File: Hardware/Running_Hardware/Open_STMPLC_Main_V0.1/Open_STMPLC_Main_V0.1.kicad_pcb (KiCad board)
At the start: 4 copper layers, 168.8 x 90 mm, 184 parts, among them J1 Conn_02x08_Odd_Even, J10 10144518-041802LF, J12 USB C, J13 RJ45_Hanrun_HR911105A_Horizon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, J2 USB C, J3 Conn_01x04, J4 TF-01A, J5 Conn_Coaxial, J6 Conn_Coaxial, J7 Simcard_Nano, J8 10144518-041802LF, J9 10144518-041802LF, Q1 DTC143Z, Q2 DTC143Z, Q3 DTC143Z, Q4 DTC143Z, Q5 DTC143Z, Q6 DTC143Z, Q7 DTC143Z, Q8 DTC143Z, SW1 Switch_6x6, SW2 SW_DIP_x01, SW3 Switch_6x6, U1 STM32F407IGTx, U10 AP63205WU, U2 ADM2587E, U3 TPS3430WDRC, U4 CH340C, U5 AMS1117-3.3, U6 W25Q64JVSSIQ, U7 LAN8720A, U8 EC200U, U9 AP63200WU, Y1 48MHz, Y2 32.768kHz, Y3 25MHz

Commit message: PCB routing completion v0.1 Main
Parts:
- added C73: 1nF/2kV, Capacitor_SMD:C_1206_3216Metric_Pad1.33x1.80mm_HandSolder, F.Cu at (209.0, 74.5)
- added D10: UAD8C05L01, Diode_SMD:D_SOD-882, F.Cu at (128.5, 72.0)
- added D11: UAD8C05L01, Diode_SMD:D_SOD-882, F.Cu at (136.5, 72.0)
- added D12: UAD8C05L01, Diode_SMD:D_SOD-882, F.Cu at (134.5, 72.0)
- added D13: UAD8C05L01, Diode_SMD:D_SOD-882, F.Cu at (144.5, 72.0)
- added D14: UAD8C05L01, Diode_SMD:D_SOD-882, F.Cu at (188.0, 66.0)
- added D15: UAD8C05L01, Diode_SMD:D_SOD-882, F.Cu at (185.5, 66.0)
- added D16: UAD8C05L01, Diode_SMD:D_SOD-882, F.Cu at (183.0, 66.0)
- added D17: UAD8C05L01, Diode_SMD:D_SOD-882, F.Cu at (180.5, 66.0)
- added D18: UAD8C05L01, Diode_SMD:D_SOD-882, F.Cu at (178.0, 66.0)
- added D19: UAD8C05L01, Diode_SMD:D_SOD-882, F.Cu at (142.5, 72.0)
- added D20: UAD8C05L01, Diode_SMD:D_SOD-882, F.Cu at (175.5, 66.0)
- added D21: UAD8C05L01, Diode_SMD:D_SOD-882, F.Cu at (173.0, 66.0)
- added D22: UAD8C05L01, Diode_SMD:D_SOD-882, F.Cu at (173.0, 68.2)
- added D23: UAD8C05L01, Diode_SMD:D_SOD-882, F.Cu at (175.5, 68.0)
- added D24: UAD8C05L01, Diode_SMD:D_SOD-882, F.Cu at (178.0, 68.0)
- added D25: UAD8C05L01, Diode_SMD:D_SOD-882, F.Cu at (180.5, 68.0)
- added D26: UAD8C05L01, Diode_SMD:D_SOD-882, F.Cu at (183.0, 68.0)
- added D27: UAD8C05L01, Diode_SMD:D_SOD-882, F.Cu at (185.5, 68.0)
- added D28: UAD8C05L01, Diode_SMD:D_SOD-882, F.Cu at (188.0, 68.0)
- added D29: UAD8C05L01, Diode_SMD:D_SOD-882, F.Cu at (199.0, 63.5)
- added D30: UAD8C05L01, Diode_SMD:D_SOD-882, F.Cu at (192.5, 63.5)
- added D31: UAD8C05L01, Diode_SMD:D_SOD-882, F.Cu at (195.0, 63.5)
- added D5: UAD8C05L01, Diode_SMD:D_SOD-882, F.Cu at (140.5, 72.0)
- added D9: UAD8C05L01, Diode_SMD:D_SOD-882, F.Cu at (130.5, 72.0)
- added FID1: Fiducial, Fiducial:Fiducial_1mm_Mask3mm, F.Cu at (53.0, 58.0)
- added FID2: Fiducial, Fiducial:Fiducial_1mm_Mask3mm, F.Cu at (213.0, 58.0)
- added FID3: Fiducial, Fiducial:Fiducial_1mm_Mask3mm, F.Cu at (206.0, 137.0)
- added FID4: Fiducial, Fiducial:Fiducial_1mm_Mask3mm, F.Cu at (53.0, 133.0)
- added R48: 10K, Resistor_SMD:R_0603_1608Metric_Pad0.98x0.95mm_HandSolder, F.Cu at (181.0, 95.5)
- added R49: 10K, Resistor_SMD:R_0603_1608Metric_Pad0.98x0.95mm_HandSolder, F.Cu at (181.0, 93.5)
- added R50: 4.7K, Resistor_SMD:R_0603_1608Metric_Pad0.98x0.95mm_HandSolder, F.Cu at (192.5, 66.5)
- added R51: 4.7K, Resistor_SMD:R_0603_1608Metric_Pad0.98x0.95mm_HandSolder, F.Cu at (195.0, 66.5)
- added R52: 4.7K, Resistor_SMD:R_0603_1608Metric_Pad0.98x0.95mm_HandSolder, F.Cu at (184.5, 71.0)
- added R53: 4.7K, Resistor_SMD:R_0603_1608Metric_Pad0.98x0.95mm_HandSolder, F.Cu at (187.0, 71.0)
- added U11: SRV05-4, Package_TO_SOT_SMD:SOT-23-6, F.Cu at (152.0, 61.5)
- added U12: SRV05-4, Package_TO_SOT_SMD:SOT-23-6, F.Cu at (164.0, 61.5)
- D2, D3, D4, D7, D8: value SMF5V0A -> UAD8C05L01; footprint Diode_SMD:D_SMF -> Diode_SMD:D_SOD-882
- D6: value DT1240A-08LP3810 -> UAD8C05L01; footprint Package_DFN_QFN:UDFN-9_1.0x3.8mm_P0.5mm -> Diode_SMD:D_SOD-882
- R30: value 10K -> 1M; footprint Resistor_SMD:R_0603_1608Metric_Pad0.98x0.95mm_HandSolder -> Resistor_SMD:R_1206_3216Metric_Pad1.30x1.75mm_HandSolder
- U7: footprint Package_DFN_QFN:VQFN-24-1EP_4x4mm_P0.5mm_EP2.5x2.5mm_ThermalVias -> Package_DFN_QFN:VQFN-24-1EP_4x4mm_P0.5mm_EP2.5x2.5mm
- moved R17 35.6 mm to (209.5, 97.5), turned to 0 degrees
- moved R30 15.7 mm to (205.0, 74.5)
- moved R32 8.51 mm to (159.0, 61.5)
- moved R25 7.65 mm to (197.5, 82.5), turned to 90 degrees
- moved R40 6.73 mm to (173.0, 71.0)
- moved C41 5.52 mm to (195.5, 82.5), turned to -90 degrees
- moved R23 5.52 mm to (195.5, 88.5), turned to 90 degrees
- moved R34 5.40 mm to (112.2, 70.8)
- moved D6 5.39 mm to (132.5, 72.0), turned to 90 degrees
- moved R41 4.92 mm to (178.0, 71.0)
- moved R39 4.53 mm to (175.5, 71.0)
- moved C71 4.30 mm to (114.0, 98.5), turned to 0 degrees
- moved C49 3.95 mm to (115.8, 70.8)
- moved C50 3.95 mm to (121.8, 70.8)
- moved C52 3.95 mm to (117.8, 70.8)
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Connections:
- net Net-(J5-In) renamed /GSM_Module/ANT_GNSS
- net Net-(J6-In) renamed /GSM_Module/ANT_MAIN
- D2 pad 1: /GSM_Module/USIM_DATA -> GND
- D2 pad 2: GND -> /GSM_Module/USIM_DATA
- D3 pad 1: /GSM_Module/USIM_DET -> GND
- D3 pad 2: GND -> /GSM_Module/USIM_DET
- D4 pad 1: /GSM_Module/USIM_RST -> GND
- D4 pad 2: GND -> /GSM_Module/USIM_RST
- D6 pad 1: /SD_DAT1 -> GND
- D6 pad 2: /SD_DAT0 -> /SD_CMD
- D7 pad 1: /GSM_Module/USIM_VDD -> GND
- D7 pad 2: GND -> /GSM_Module/USIM_VDD
- D8 pad 1: /GSM_Module/USIM_CLK -> GND
- D8 pad 2: GND -> /GSM_Module/USIM_CLK
- J1 pad 11: /Microcontroller/EX_SPI_CLK -> /Microcontroller/EX_SPI_MISO
- J1 pad 12: /Microcontroller/EX_GPIO2 -> /Microcontroller/EX_SPI_CLK
- J1 pad 13: unconnected-(J1-Pin_13-Pad13) -> /Microcontroller/EX_UART_RX
- J1 pad 14: unconnected-(J1-Pin_14-Pad14) -> /Microcontroller/EX_UART_TX
- J1 pad 2: +3V3 -> +5V
- J1 pad 3: /Microcontroller/EX_I2C_SDA -> /Microcontroller/EX_I2C_SCL
- J1 pad 4: unconnected-(J1-Pin_4-Pad4) -> /Microcontroller/EX_I2C_SDA
- J1 pad 5: /Microcontroller/EX_I2C_SCL -> /Microcontroller/EX_GPIO4
- J1 pad 6: /Microcontroller/EX_UART_TX -> /Microcontroller/EX_GPIO5
- J1 pad 7: /Microcontroller/EX_SPI_MOSI -> /Microcontroller/EX_GPIO2
- J1 pad 8: /Microcontroller/EX_UART_RX -> /Microcontroller/EX_GPIO3
- J1 pad 9: /Microcontroller/EX_SPI_MISO -> /Microcontroller/EX_SPI_MOSI
- J12 pad A4: Net-(J12-VBUS-PadA4) -> VBUS
- J12 pad A9: Net-(J12-VBUS-PadA4) -> VBUS
- J12 pad B4: Net-(J12-VBUS-PadA4) -> VBUS
- J12 pad B9: Net-(J12-VBUS-PadA4) -> VBUS
- J13 pad 10: /Ethernet/LED2 -> GND
- J13 pad 11: /Ethernet/LED1 -> GND
- J13 pad 8: Earth -> Net-(C73-Pad1)
- J13 pad SH: GND -> Net-(C73-Pad1)
- J2 pad A4: Net-(J2-VBUS-PadA4) -> VBUS
- J2 pad A9: Net-(J2-VBUS-PadA4) -> VBUS
- J2 pad B4: Net-(J2-VBUS-PadA4) -> VBUS
- J2 pad B9: Net-(J2-VBUS-PadA4) -> VBUS
- R17 pad 1: /Microcontroller/DISP_SCL -> GND
- R17 pad 2: +3V3 -> /Ethernet/LED2
- R27 pad 2: +3V3 -> /Ethernet/LED1
- R28 pad 2: +3V3 -> /Ethernet/LED2
- R30 pad 1: /Microcontroller/DISP_SDA -> GND
- R30 pad 2: +3V3 -> Net-(C73-Pad1)
- R32 pad 1: Net-(J12-VBUS-PadA4) -> VBUS
- R9 pad 1: Net-(J2-VBUS-PadA4) -> VBUS
- U1 pad 100: unconnected-(U1-PD12-Pad100) -> /GSM_Module/RESET_IN
- U1 pad 101: unconnected-(U1-PD13-Pad101) -> /GSM_Module/PWRKEY_IN
- U1 pad 104: unconnected-(U1-PD14-Pad104) -> /SD_DET
- U1 pad 45: /B2B_Connector/DIG_OUT_5 -> /Microcontroller/EX_I2C_SCL
- U1 pad 46: /B2B_Connector/DIG_OUT_~{FAULT}_7 -> /Microcontroller/EX_I2C_SDA
- U1 pad 7: unconnected-(U1-PI8-Pad7) -> /Microcontroller/WDI
- U1 pad 77: unconnected-(U1-PE14-Pad77) -> /MODBUS/RS485_DE
- U1 pad 78: unconnected-(U1-PE15-Pad78) -> /MODBUS/RS485_~{RE}
- U1 pad 83: unconnected-(U1-PH6-Pad83) -> /B2B_Connector/DIG_OUT_~{FAULT}_7
- U1 pad 84: unconnected-(U1-PH7-Pad84) -> /Microcontroller/DISP_SCL
- U1 pad 85: unconnected-(U1-PH8-Pad85) -> /Microcontroller/DISP_SDA
- U1 pad 86: unconnected-(U1-PH9-Pad86) -> /B2B_Connector/DIG_OUT_5
- U1 pad 87: unconnected-(U1-PH10-Pad87) -> /Microcontroller/EX_GPIO5
- U1 pad 88: unconnected-(U1-PH11-Pad88) -> /Microcontroller/EX_GPIO4
- U1 pad 89: unconnected-(U1-PH12-Pad89) -> /Microcontroller/EX_GPIO3
- U1 pad 92: unconnected-(U1-PB12-Pad92) -> /Microcontroller/EX_GPIO2
- U1 pad 93: unconnected-(U1-PB13-Pad93) -> /Microcontroller/EX_GPIO1
- U1 pad 96: unconnected-(U1-PD8-Pad96) -> /Microcontroller/Flash_Hold
- U1 pad 97: unconnected-(U1-PD9-Pad97) -> /Microcontroller/Flash_CS
- U1 pad 98: unconnected-(U1-PD10-Pad98) -> /Microcontroller/Flash_WP
- U1 pad 99: unconnected-(U1-PD11-Pad99) -> /GSM_Module/GSM_BOOT
- U7 pad 10: /Ethernet/ETH_RXER -> /Ethernet/PHYAD0
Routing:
- net +3V3: track 22.9 -> 364.5 mm, vias 0 -> 20
- net +5V: track 18.1 -> 250.7 mm, vias 0 -> 3
- net /Microcontroller/3V3_MCU: track 89.2 -> 245.8 mm, vias 0 -> 4
- net /GSM_Module/GSM_DN: track 0.00 -> 117.3 mm, vias 0 -> 2
- net /GSM_Module/GSM_DP: track 0.00 -> 117.2 mm, vias 0 -> 2
- net /GSM_Module/SIM_TX: track 5.05 -> 94.3 mm, vias 1 -> 2
- net /GSM_Module/SIM_RX: track 4.40 -> 84.6 mm, vias 1 -> 2
- net GND: track 4.40 -> 79.4 mm, vias 0 -> 202
- net /Microcontroller/EX_I2C_SDA: track 0.00 -> 71.4 mm, vias 0 -> 2
- net /Microcontroller/EX_I2C_SCL: track 0.00 -> 69.1 mm, vias 0 -> 2
- net +24V: track 20.6 -> 88.0 mm, vias 1 -> 3
- net Net-(J13-RCT): track 0.00 -> 64.3 mm, vias 0 -> 5
- net /GSM_Module/PWRKEY_IN: track 0.00 -> 63.1 mm, vias 0 -> 2
- net /GSM_Module/RESET_IN: track 0.00 -> 60.6 mm, vias 0 -> 2
- net /GSM_Module/GSM_BOOT: track 0.00 -> 59.6 mm, vias 0 -> 2
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- added copper zone on In1.Cu, net +3V3
- added copper zone on B.Cu, net GND
- added copper zone on F.Cu, net GND
- added copper zone on In1.Cu, net GND
- added copper zone on In2.Cu, net GND
- added copper zone on F.Cu, net Net-(C73-Pad1)
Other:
- board text added: "Open_STMPLC_Main_V0.1"

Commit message: Silkscreen and DRC
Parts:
- added G***: LOGO, Logo:Thingslista, F.Cu at (186.0, 131.0)
- added J11: Conn_01x05, Connector_PinHeader_2.54mm:PinHeader_1x05_P2.54mm_Vertical, F.Cu at (155.9, 135.5)
- J10, J8, J9: value 10144518-041802LF -> 10144518-043802LF
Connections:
- U1 pad 124: /B2B_Connector/DIG_IN_5 -> /Microcontroller/SWDIO
- U1 pad 137: /B2B_Connector/RTD_~{CS}_1 -> /Microcontroller/SWCLK
- U1 pad 142: unconnected-(U1-PD0-Pad142) -> /B2B_Connector/RTD_~{CS}_1
- U1 pad 173: unconnected-(U1-PI4-Pad173) -> /B2B_Connector/DIG_IN_5
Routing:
- net /Microcontroller/SWCLK: track 0.00 -> 84.7 mm, vias 0 -> 1
- net /Microcontroller/SWDIO: track 0.00 -> 78.0 mm, vias 0 -> 1
- net /Ethernet/ETH_CRSDV: track 27.3 -> 71.9 mm
- net /Ethernet/ETH_RXD0: track 32.1 -> 71.9 mm
- net /Ethernet/ETH_RXD1: track 33.0 -> 71.9 mm
- net /Ethernet/ETH_REFCLKO: track 38.5 -> 71.9 mm
- net /B2B_Connector/DIG_IN_5: track 108.2 -> 134.8 mm
- net /Microcontroller/3V3_MCU: track 245.8 -> 264.2 mm, vias 4 -> 5
- net GND: track 79.4 -> 71.7 mm, vias 202 -> 191
- net /Microcontroller/~{STM_RST}: track 37.6 -> 44.9 mm
- net /B2B_Connector/RTD_~{CS}_2: track 104.8 -> 102.2 mm
- net /B2B_Connector/RTD_~{CS}_1: track 101.3 -> 103.8 mm
- net /Microcontroller/DEBUG_DN: track 20.9 -> 23.4 mm
- net /B2B_Connector/THRM_~{DRDY}: track 102.1 -> 99.6 mm
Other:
- board text added: "BOOT"
- board text added: "ETHERNET"
- board text added: "GND RX MISO MOSI IO2 IO4 SCL 3V3"
- board text added: "GND TX SCLK IO1 IO3 IO5 SDA 5V"
- board text added: "PWRKEY"
- board text added: "RESET"
- board text added: "RST DIO GND CLK 3V3"
- board text added: "RST SWDIO GND SWCLK 3V3"
- board text added: "SDA SCL GND 3V3"
- board text added: "SD_MICRO"
- board text added: "SIM_NANO"
- board text added: "TTL DEBUG"
- board text added: "USB"

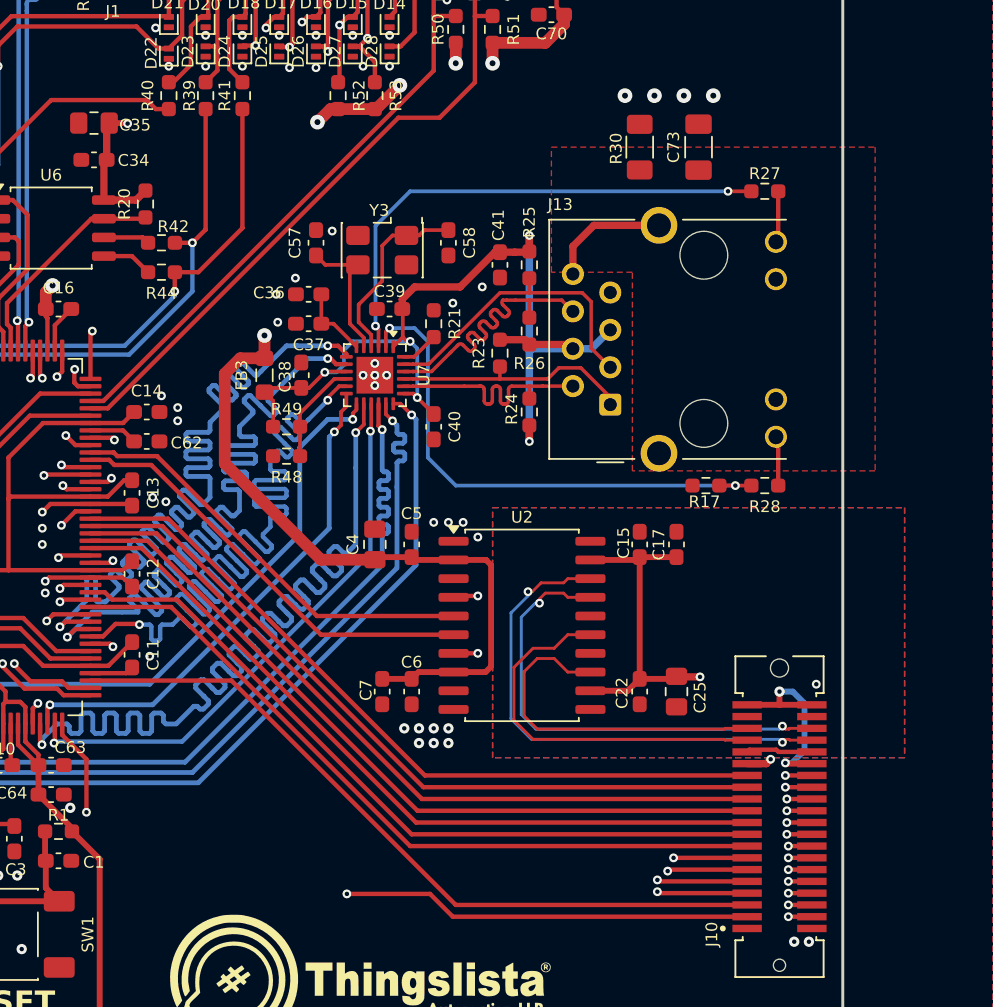
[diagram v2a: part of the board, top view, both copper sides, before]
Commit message: Ethernet updated to vertical
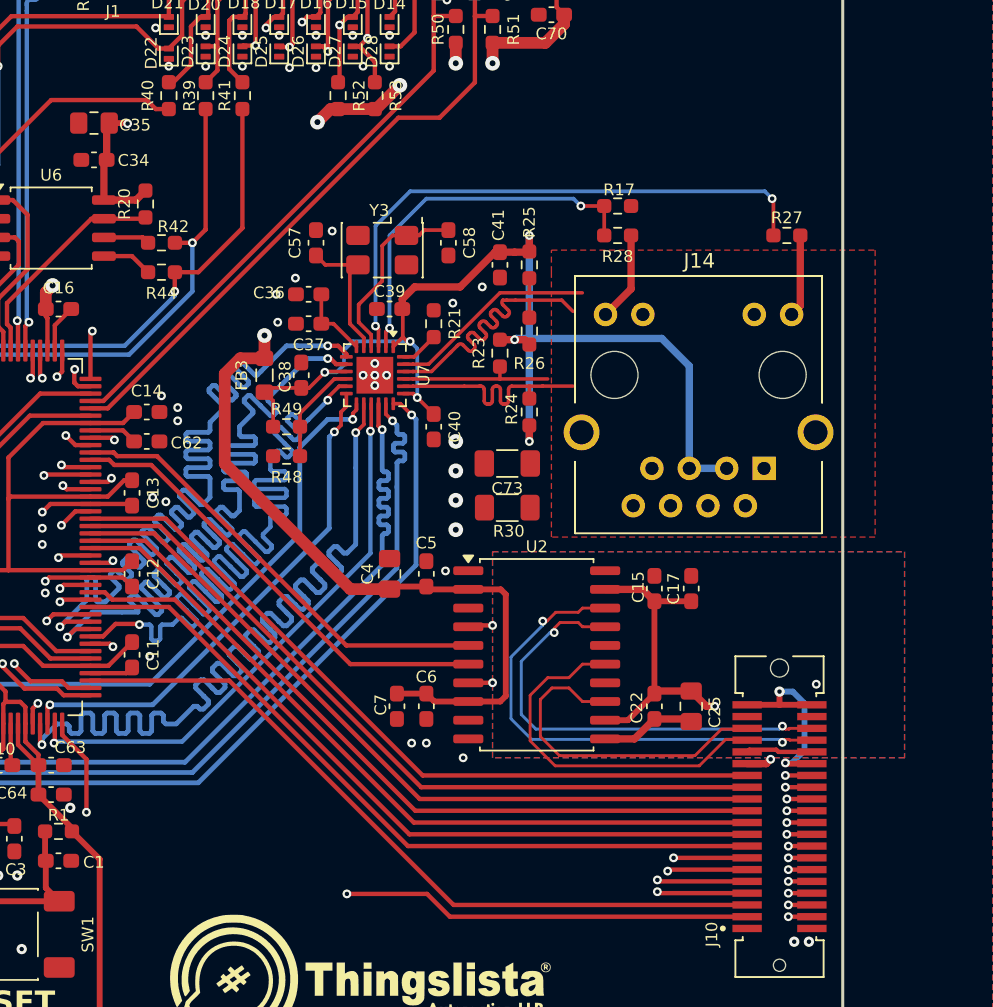
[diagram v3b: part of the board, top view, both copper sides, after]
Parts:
- removed J13: RJ45_Hanrun_HR911105A_Horizontal, Connector_RJ:RJ45_Hanrun_HR911105A_Horizontal
- added J14: HY951180A, HY951180A:HY951180A, F.Cu at (213.5, 96.3)
- moved R30 26.1 mm to (196.0, 99.0), turned to 0 degrees
- moved C73 25.1 mm to (196.0, 96.0), turned to 180 degrees
- moved R17 19.9 mm to (203.5, 78.5), turned to 180 degrees
- moved R28 19.7 mm to (203.5, 80.5)
- moved R27 3.35 mm to (215.0, 80.5)
- moved C15 3.16 mm to (206.0, 104.5)
- moved C17 3.16 mm to (208.5, 104.5)
- moved C4 2.24 mm to (188.0, 103.5)
- moved C5 2.24 mm to (190.5, 103.5)
- moved U2 2.24 mm to (198.0, 109.0)
- moved C22 1.41 mm to (206.0, 112.5)
- moved C25 1.41 mm to (208.5, 112.5)
- moved C6 1.41 mm to (190.5, 112.5)
- moved C7 1.41 mm to (188.5, 112.5)
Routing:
- net Net-(J14-RCT): track 64.3 -> 77.2 mm, vias 5 -> 6
- net /Ethernet/LED2: track 36.1 -> 25.5 mm
- net Net-(C73-Pad1): track 8.32 -> 0.00 mm
- net GND_MODBUS: track 4.52 -> 11.0 mm
- net /Ethernet/TD+: track 16.5 -> 10.7 mm
- net /Ethernet/RD+: track 21.0 -> 15.2 mm
- net /B2B_Connector/3V3_ISO: track 33.1 -> 28.2 mm
- net /Ethernet/LED1: track 34.8 -> 39.0 mm
- net Net-(J14-Pad12): track 3.38 -> 6.09 mm
- net Net-(J14-Pad9): track 3.50 -> 5.61 mm
- net +3V3: track 364.5 -> 366.3 mm
- net /MODBUS/RS485_TXD: track 37.7 -> 39.6 mm
- net /MODBUS/RS485_~{RE}: track 29.3 -> 31.1 mm
- net /MODBUS/RS485_RXD: track 32.5 -> 34.3 mm
- net /MODBUS/RS485_DE: track 29.6 -> 31.4 mm
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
